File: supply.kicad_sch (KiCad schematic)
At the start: 98 parts, among them IC12 74HC00PW, IC13 SN74LVC1G126DCKR, IC4 TPS7A0518PDBVT, J12 533980471, T3 BSS138APW, U1 LM3671MF-3.3/NOPB, U2 LM62440-Q1, U3 SN74LXC1T45DBVR, U5 LM3671MF-3.3/NOPB, U6 SIC477ED-T1-GE3

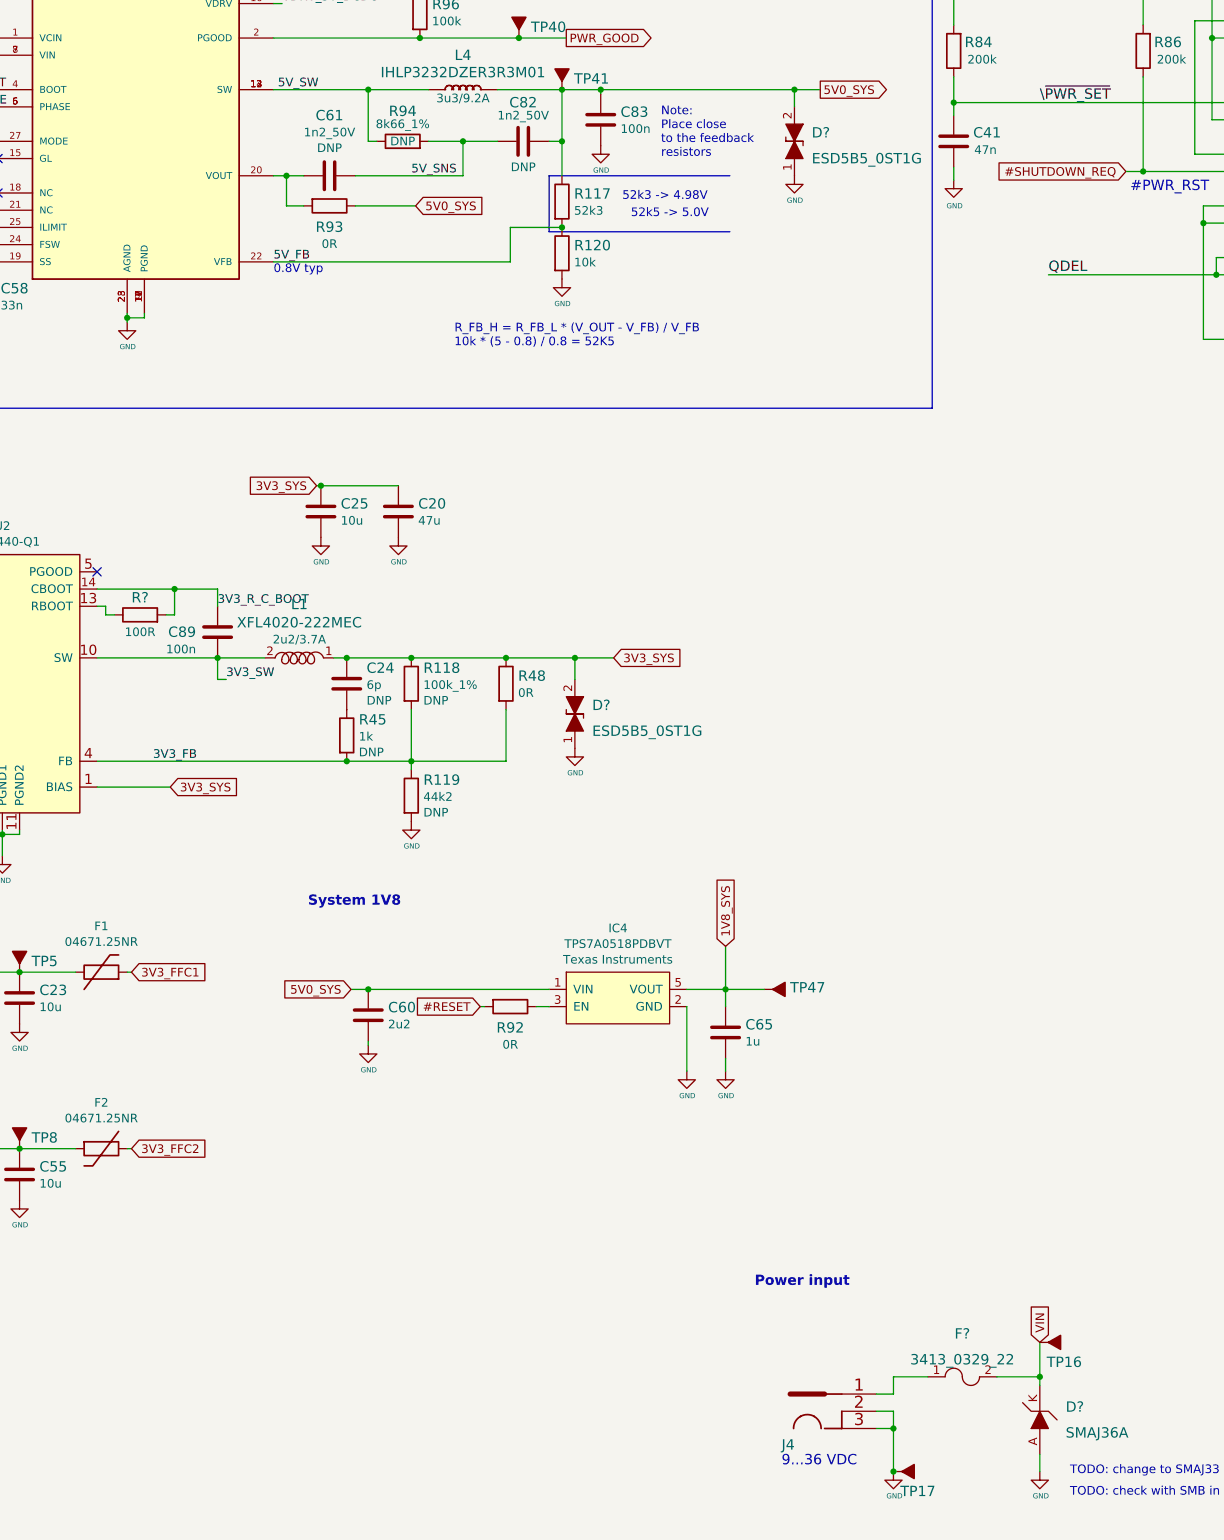
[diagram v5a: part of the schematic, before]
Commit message: Resolve TOOD on USB sheet
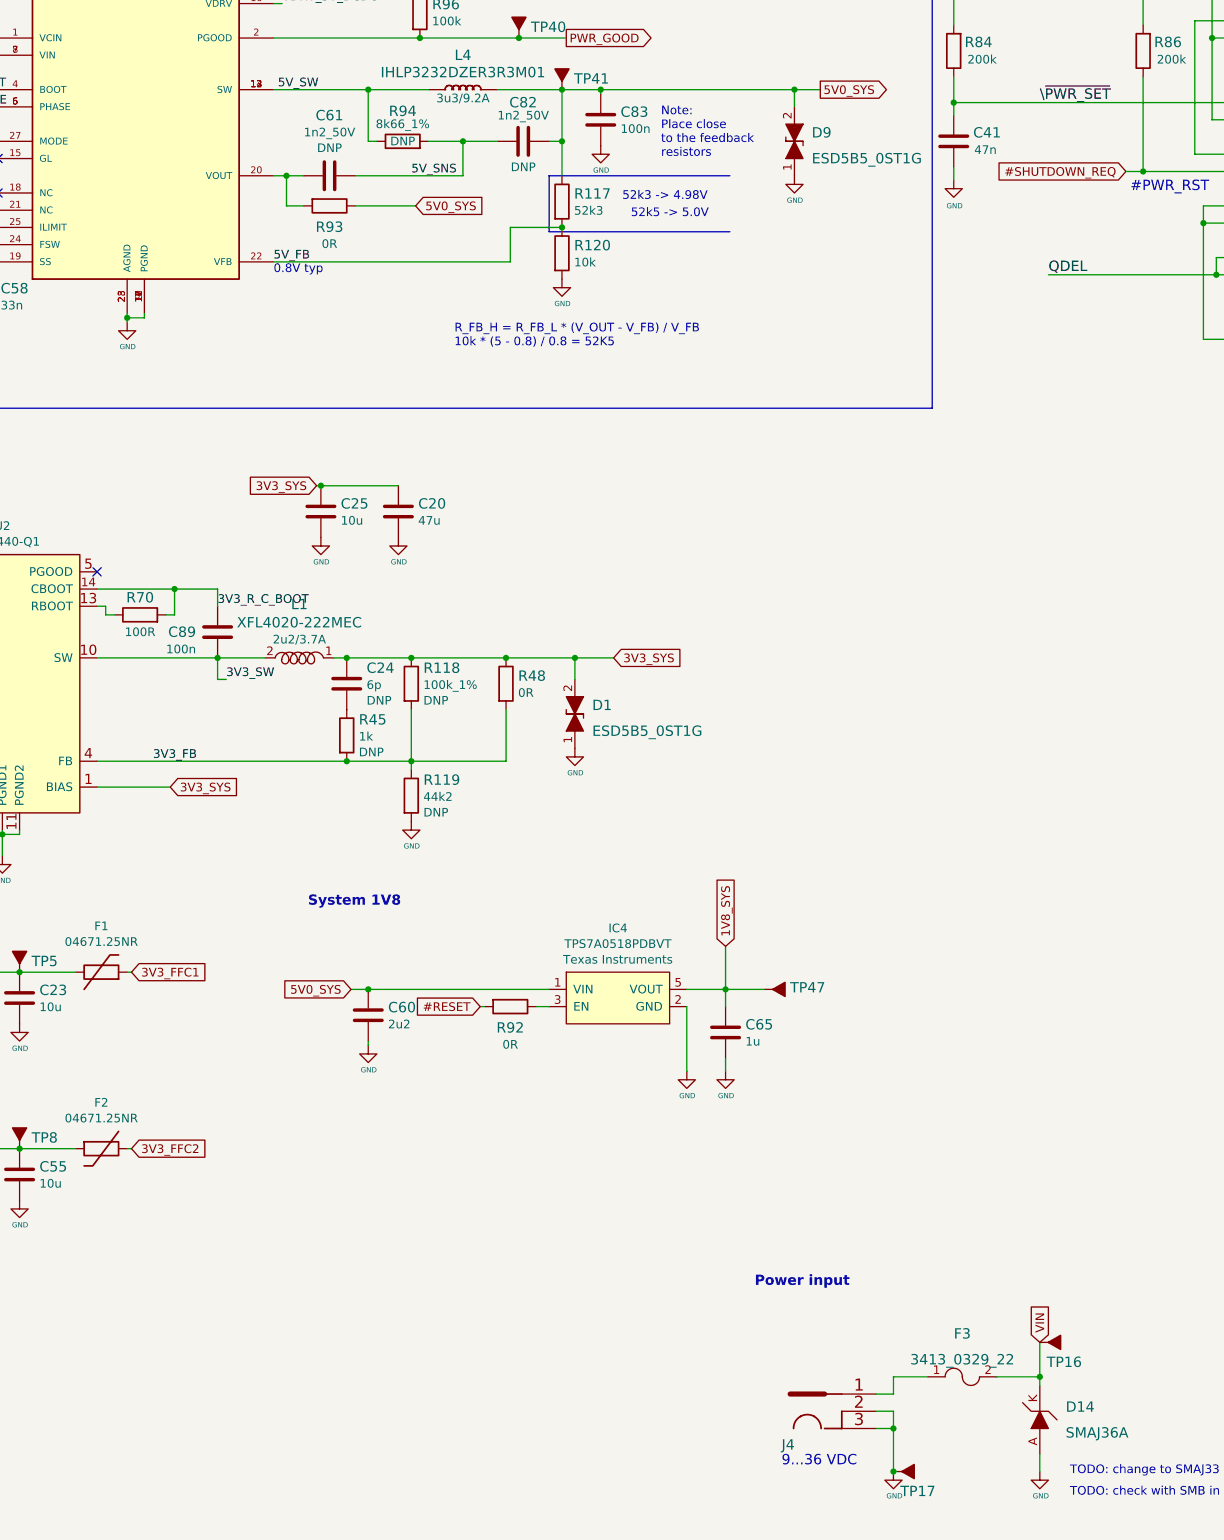
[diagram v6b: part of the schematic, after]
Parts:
- gave numbers to parts that had none: 5
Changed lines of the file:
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@@
   (symbol (lib_id "jetson-nano-baseboard:R_100R_0402") (at 120.015 137.795 0) (unit 1)
     (in_bom yes) (on_board yes)
-    (property "Reference" "R?" (id 0) (at 120.015 135.255 0)
+    (property "Reference" "R70" (id 0) (at 120.015 135.255 0)
       (effects (font (size 1.524 1.524)))
     )
@@
   (symbol (lib_id "jetson-nano-baseboard:SMAJ36A") (at 252.73 256.54 90) (unit 1)
     (in_bom yes) (on_board yes) (fields_autoplaced)
-    (property "Reference" "D?" (id 0) (at 256.54 254.635 90)
+    (property "Reference" "D14" (id 0) (at 256.54 254.635 90)
       (effects (font (size 1.524 1.524)) (justify right))
     )
@@
   (symbol (lib_id "jetson-nano-baseboard:ESD5B5_0ST1G") (at 216.535 67.945 90) (unit 1)
     (in_bom yes) (on_board yes) (fields_autoplaced)
-    (property "Reference" "D?" (id 0) (at 219.075 66.675 90)
+    (property "Reference" "D9" (id 0) (at 219.075 66.675 90)
       (effects (font (size 1.524 1.524)) (justify right))
     )
@@
   (symbol (lib_id "jetson-nano-baseboard:3413_0329_22") (at 241.3 250.19 0) (unit 1)
     (in_bom yes) (on_board yes) (fields_autoplaced)
-    (property "Reference" "F?" (id 0) (at 241.3 243.84 0)
+    (property "Reference" "F3" (id 0) (at 241.3 243.84 0)
       (effects (font (size 1.524 1.524)))
     )
@@
   (symbol (lib_id "jetson-nano-baseboard:GND") (at 216.535 73.025 0) (unit 1)
     (in_bom yes) (on_board yes)
-    (property "Reference" "#GND_?" (id 0) (at 216.535 73.025 0)
+    (property "Reference" "#GND_0168" (id 0) (at 216.535 73.025 0)
       (effects (font (size 0.508 0.508)) hide)
     )
@@
   (symbol (lib_id "jetson-nano-baseboard:ESD5B5_0ST1G") (at 184.15 152.4 90) (unit 1)
     (in_bom yes) (on_board yes) (fields_autoplaced)
-    (property "Reference" "D?" (id 0) (at 186.69 151.13 90)
+    (property "Reference" "D1" (id 0) (at 186.69 151.13 90)
       (effects (font (size 1.524 1.524)) (justify right))
     )
@@
   (symbol (lib_id "jetson-nano-baseboard:GND") (at 252.73 264.16 0) (unit 1)
     (in_bom yes) (on_board yes)
-    (property "Reference" "#GND_?" (id 0) (at 252.73 264.16 0)
+    (property "Reference" "#GND_0116" (id 0) (at 252.73 264.16 0)
       (effects (font (size 0.508 0.508)) hide)
     )
@@
   (symbol (lib_id "jetson-nano-baseboard:GND") (at 184.15 157.48 0) (unit 1)
     (in_bom yes) (on_board yes)
-    (property "Reference" "#GND_?" (id 0) (at 184.15 157.48 0)
+    (property "Reference" "#GND_0113" (id 0) (at 184.15 157.48 0)
       (effects (font (size 0.508 0.508)) hide)
     )
